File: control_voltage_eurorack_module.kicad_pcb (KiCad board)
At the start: 2 copper layers, 71.1 x 110 mm, 51 parts, among them J1 Conn_02x08_Odd_Even, J2 AVR-ISP-6, J3 Conn_01x04, J4 TrigOut, J5 GateOut, J6 ExtClkIn, J7 Conn_01x03, J8 CVOut, SW1 Menu_Encoder, U1 TL072, U2 ATmega16A-AU, U3 MCP4725xxx-xCH, Y1 16M

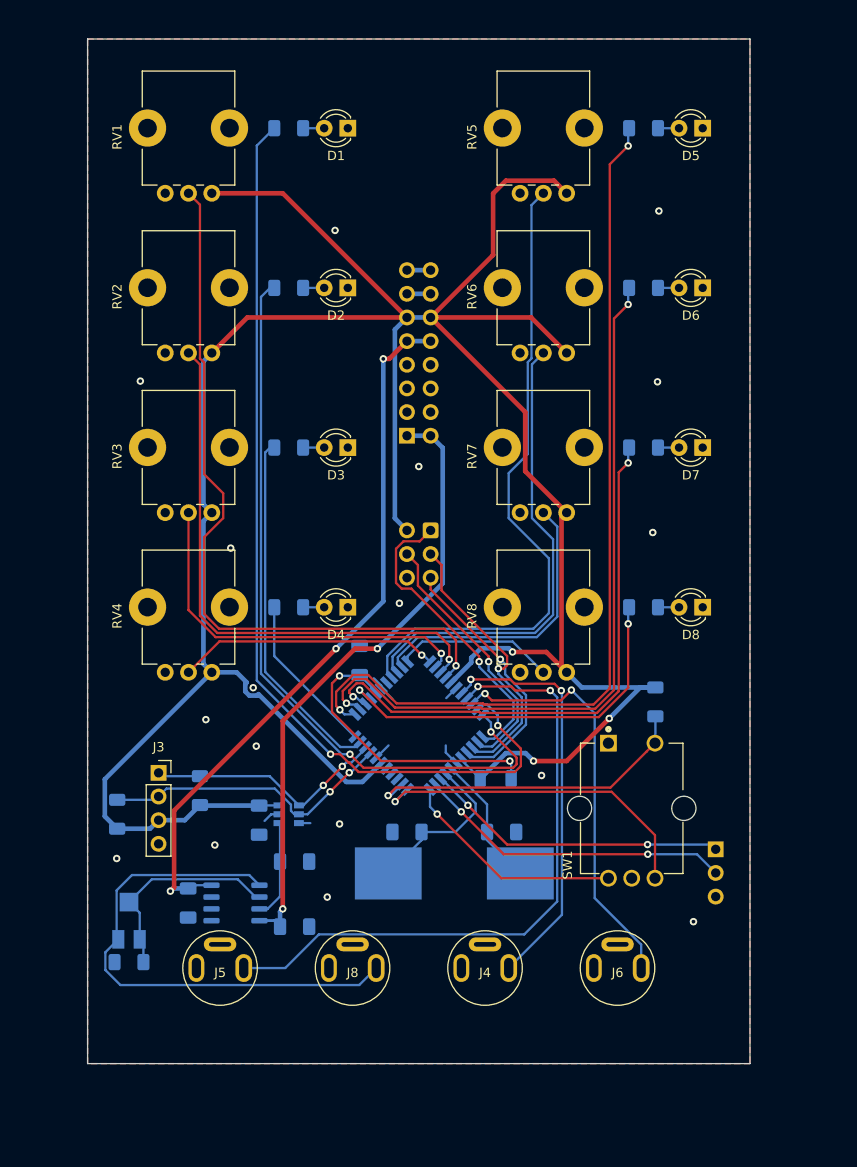
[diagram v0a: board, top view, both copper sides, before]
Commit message: updated to kicad 6
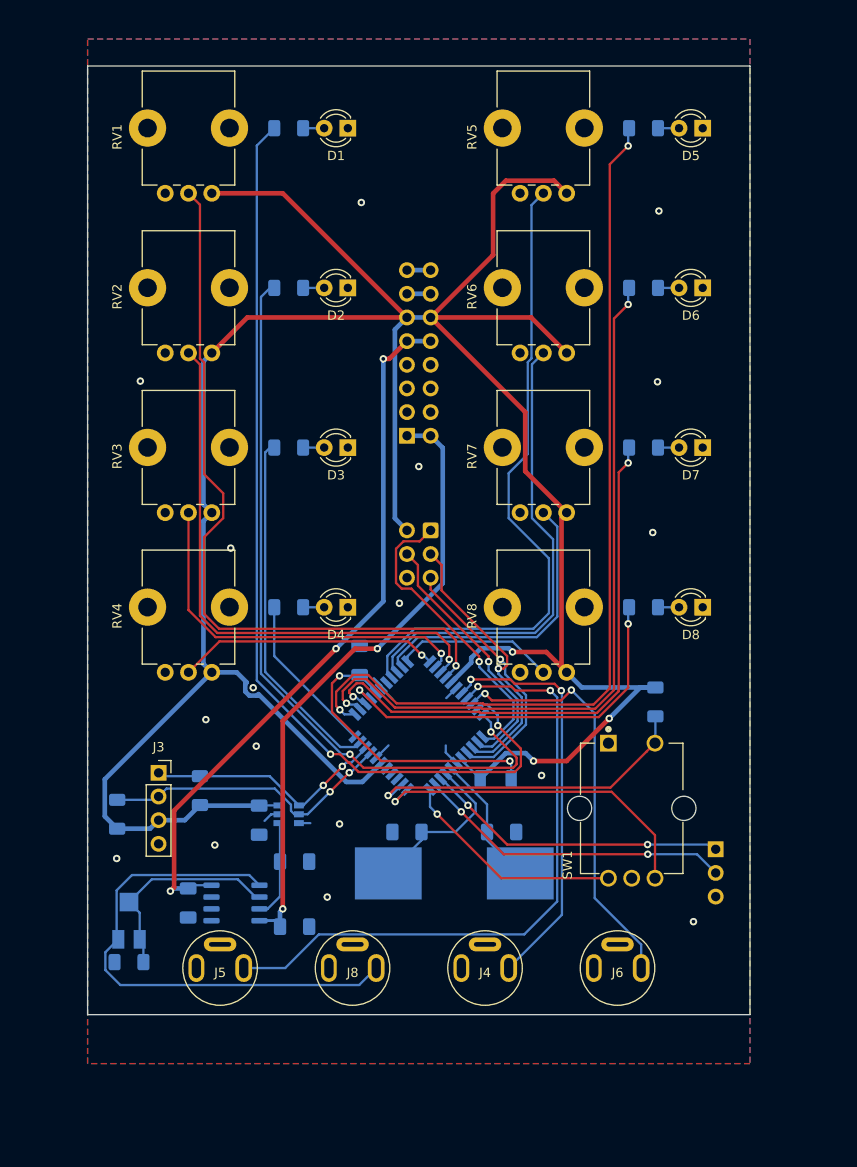
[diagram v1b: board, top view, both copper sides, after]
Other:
- board size 71.1 x 110 mm -> 71.1 x 101.9 mm
- net class Default removed

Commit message: added schematic
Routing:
- net GND: track 11.9 -> 48.4 mm, vias 17 -> 16
- net SCL: track 32.7 -> 32.0 mm
